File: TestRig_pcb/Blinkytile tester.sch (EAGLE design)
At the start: 142 parts, among them IC1 LM317BD2T, IC10 LM317BD2T, IC11 LM317BD2T, IC12 LM317BD2T, IC13 LM317BD2T, IC14 LM317BD2T, IC15 LM317BD2T, IC16 LM317BD2T, IC2 LM317BD2T, IC3 LM317BD2T, IC4 LM317BD2T, IC5 LM317BD2T, IC6 LM317BD2T, IC7 LM317BD2T, IC8 LM317BD2T, IC9 LM317BD2T, X1 MINI-USB_4P-85-32004-10X

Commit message: RevB of tester board: add 5v buffers
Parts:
- removed C1, C10, C11, C12, C13, C14, C15, C16, C17, C18, C19, C2, C20, C21, C22, C23, C24, C25, C26, C27, C28, C29, C3, C30, C31, C32, C4, C5, C6, C7, C8, C9: 0.1uF, rcl:C-EUC0805
- removed IC1, IC10, IC11, IC12, IC13, IC14, IC15, IC16, IC2, IC3, IC4, IC5, IC6, IC7, IC8, IC9: LM317BD2T, v-reg:LM317BD2T
- removed LED1, LED10, LED11, LED12, LED13, LED14, LED15, LED16, LED2, LED3, LED4, LED5, LED6, LED7, LED8, LED9: RED, adafruit:LED5MM
- removed R15, R16, R17, R18, R19, R20, R21, R22, R23, R24, R25, R26, R27, R28, R29, R30, R31, R32: (no value), rcl:R-EU_M0805
- removed SL16, SL17: (no value), con-amp-quick:M04
- removed TP1, TP10, TP11, TP12, TP13, TP14, TP15, TP16, TP2, TP3, TP4, TP5, TP6, TP7, TP8, TP9: TPPAD1-13Y, testpad:TPPAD1-13Y
- added SW1: SPST_TACT-EVQQ2, adafruit:SPST_TACT-EVQQ2
- added T1: (no value), zetex:PMOSSOT223
- added U1, U3: SN74HCT245PWR, scanlime:74245PW
- R1, R10, R11, R12, R13, R14, R2, R3, R4, R5, R6, R7, R8, R9: value (none) -> 50; device rcl:R-EU_M0805 -> adafruit:R-US_R0603
- renumbered LED17 to PASS, LED18 to FAIL, SL10 to OUT_9, SL11 to OUT_10, SL12 to OUT_11, SL13 to OUT_12, SL14 to OUT_13, SL15 to OUT_14, SL18 to SWITCH, SL2 to OUT_1, SL3 to OUT_2, SL4 to OUT_3, SL5 to OUT_4, SL6 to OUT_5, SL7 to OUT_6, SL8 to OUT_7, SL9 to OUT_8
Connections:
- net N$51 renamed GOOD
- removed net ADDR15: SL16.2, U$1.2
- removed net ADDR16: SL17.2, U$1.1
- removed net N$10: IC4.OUT, R7.1
- removed net N$12: LED4.C, R8.2
- removed net N$13: IC5.OUT, R9.1
- removed net N$14: C9.1, IC5.ADJ, LED5.A, OUT_5.1, R9.2, TP5.TP
- removed net N$15: LED5.C, R10.2
- removed net N$16: IC6.OUT, R11.1
- removed net N$18: LED6.C, R12.2
- removed net N$19: IC7.OUT, R13.1
- removed net N$21: LED7.C, R14.2
- removed net N$22: IC8.OUT, R15.1
- removed net N$24: LED8.C, R16.2
- removed net N$25: IC9.OUT, R17.1
- removed net N$27: LED9.C, R18.2
- removed net N$28: IC10.OUT, R19.1
- removed net N$30: LED10.C, R20.2
- removed net N$31: IC11.OUT, R21.1
- removed net N$33: LED11.C, R22.2
- removed net N$34: IC12.OUT, R23.1
- removed net N$35: C23.1, IC12.ADJ, LED12.A, OUT_12.1, R23.2, TP12.TP
- removed net N$36: LED12.C, R24.2
- removed net N$37: IC13.OUT, R25.1
- removed net N$39: LED13.C, R26.2
- removed net N$40: IC14.OUT, R27.1
- removed net N$42: LED14.C, R28.2
- removed net N$43: IC15.OUT, R29.1
- removed net N$45: LED15.C, R30.2
- removed net N$46: IC16.OUT, R31.1
- removed net N$47: C31.1, IC16.ADJ, LED16.A, R31.2, SL17.1, TP16.TP
- removed net N$48: LED16.C, R32.2
- removed net N$5: LED1.C, R2.2
- removed net N$54: SWITCH.2, U$1.9
- removed net N$6: LED2.C, R4.2
- removed net N$7: IC3.OUT, R5.1
- removed net N$9: LED3.C, R6.2
- new net 5V_B: R1.1, R10.1, R11.1, R12.1, R13.1, R14.1, R2.1, R3.1, R4.1, R5.1, R6.1, R7.1, R8.1, R9.1, T1.D
- new net ADDR10_B: OUT_10.2, U1.B2
- new net ADDR11_B: OUT_11.2, U1.B3
- new net ADDR12_B: OUT_12.2, U1.B4
- new net ADDR13_B: OUT_13.2, U1.B5
- new net ADDR14_B: OUT_14.2, U1.B6
- new net ADDR1_B: OUT_1.2, U3.B1
- new net ADDR2_B: OUT_2.2, U3.B2
- new net ADDR3_B: OUT_3.2, U3.B3
- new net ADDR4_B: OUT_4.2, U3.B4
- new net ADDR5_B: OUT_5.2, U3.B5
- new net ADDR6_B: OUT_6.2, U3.B6
- new net ADDR7_B: OUT_7.2, U3.B7
- new net ADDR8_B: OUT_8.2, U3.B8
- new net ADDR9_B: OUT_9.2, U1.B1
- new net DATA_B: OUT_1.3, OUT_10.3, OUT_11.3, OUT_12.3, OUT_13.3, OUT_14.3, OUT_2.3, OUT_3.3, OUT_4.3, OUT_5.3, OUT_6.3, OUT_7.3, OUT_8.3, OUT_9.3, U1.B8
- new net PWR_EN: U$1.2, U1.A7
- new net PWR_EN_B: T1.G, U1.B7
- net +5V: now also T1.S, U1.DIR, U1.OE, U1.VCC, U3.DIR, U3.OE, U3.VCC; no longer C1.1, C10.1, C12.1, C14.1, C16.1, C18.1, C20.1, C22.1, C24.1, C26.1, C28.1, C30.1, C32.1, C4.1, C6.1, C8.1, IC1.IN, IC10.IN, IC11.IN, IC12.IN, IC13.IN, IC14.IN, IC15.IN, IC16.IN, IC2.IN, IC3.IN, IC4.IN, IC5.IN, IC6.IN, IC7.IN, IC8.IN, IC9.IN
- net ADDR1: now also U3.A1; no longer OUT_1.2
- net ADDR10: now also U1.A2; no longer OUT_10.2
- net ADDR11: now also U1.A3; no longer OUT_11.2
- net ADDR12: now also U1.A4; no longer OUT_12.2
- net ADDR13: now also U1.A5; no longer OUT_13.2
- net ADDR14: now also U1.A6; no longer OUT_14.2
- net ADDR2: now also U3.A2; no longer OUT_2.2
- net ADDR3: now also U3.A3; no longer OUT_3.2
- net ADDR4: now also U3.A4; no longer OUT_4.2
- net ADDR5: now also U3.A5; no longer OUT_5.2
- net ADDR6: now also U3.A6; no longer OUT_6.2
- net ADDR7: now also U3.A7; no longer OUT_7.2
- net ADDR8: now also U3.A8; no longer OUT_8.2
- net ADDR9: now also U1.A1; no longer OUT_9.2
- net DATA: now also U1.A8; no longer OUT_1.3, OUT_10.3, OUT_11.3, OUT_12.3, OUT_13.3, OUT_14.3, OUT_2.3, OUT_3.3, OUT_4.3, OUT_5.3, OUT_6.3, OUT_7.3, OUT_8.3, OUT_9.3, SL16.3, SL17.3
- net GND: now also SW1.P, SW1.P1, U1.GND, U3.GND; no longer C1.2, C10.2, C11.2, C12.2, C13.2, C14.2, C15.2, C16.2, C17.2, C18.2, C19.2, C2.2, C20.2, C21.2, C22.2, C23.2, C24.2, C25.2, C26.2, C27.2, C28.2, C29.2, C3.2, C30.2, C31.2, C32.2, C4.2, C5.2, C6.2, C7.2, C8.2, C9.2, R10.1, R12.1, R14.1, R16.1, R18.1, R2.1, R20.1, R22.1, R24.1, R26.1, R28.1, R30.1, R32.1, R4.1, R6.1, R8.1, SL16.4, SL17.4
- net N$1: now also OUT_5.1, R5.2; no longer IC1.OUT, R1.1
- net N$11: now also R4.2; no longer C7.1, IC4.ADJ, LED4.A, R7.2, TP4.TP
- net N$17: now also R6.2; no longer C11.1, IC6.ADJ, LED6.A, R11.2, TP6.TP
- net N$2: no longer C2.1, IC1.ADJ, LED1.A, TP1.TP
- net N$20: now also R7.2; no longer C13.1, IC7.ADJ, LED7.A, R13.2, TP7.TP
- net N$23: now also R8.2; no longer C15.1, IC8.ADJ, LED8.A, R15.2, TP8.TP
- net N$26: now also R9.2; no longer C17.1, IC9.ADJ, LED9.A, R17.2, TP9.TP
- net N$29: now also R10.2; no longer C19.1, IC10.ADJ, LED10.A, R19.2, TP10.TP
- net N$3: now also SW1.S, SW1.S1, SWITCH.2, U$1.9; no longer IC2.OUT, R3.1
- net N$32: now also R11.2; no longer C21.1, IC11.ADJ, LED11.A, R21.2, TP11.TP
- net N$38: now also R13.2; no longer C25.1, IC13.ADJ, LED13.A, R25.2, TP13.TP
- net N$4: now also R2.2; no longer C3.1, IC2.ADJ, LED2.A, R3.2, TP2.TP
- net N$41: now also R14.2; no longer C27.1, IC14.ADJ, LED14.A, R27.2, TP14.TP
- net N$44: now also OUT_12.1, R12.2; no longer C29.1, IC15.ADJ, LED15.A, R29.2, SL16.1, TP15.TP
- net N$8: now also R3.2; no longer C5.1, IC3.ADJ, LED3.A, R5.2, TP3.TP

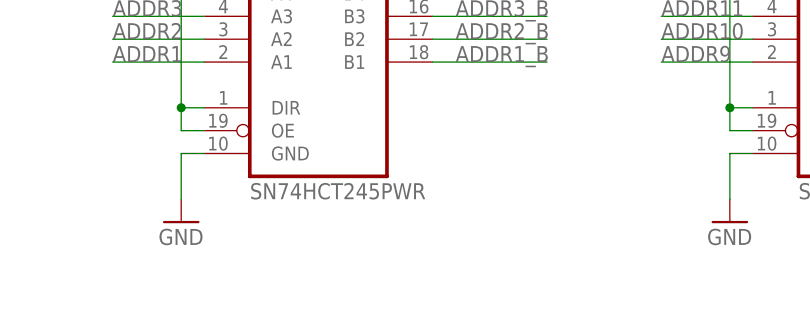
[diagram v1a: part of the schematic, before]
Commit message: Getting the tile test rig working: small circuit design issues.
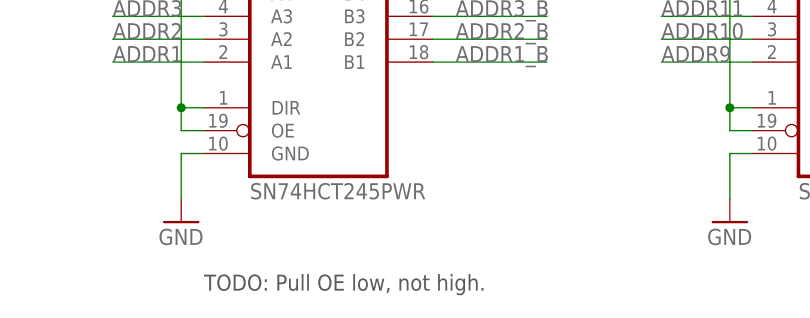
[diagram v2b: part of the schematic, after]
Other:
- note added: "TODO: Pull OE low, not high."
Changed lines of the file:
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@@
 <sheet>
 <plain>
+<text x="-20.32" y="-101.6" size="1.778" layer="97">TODO: Pull OE low, not high.</text>
 </plain>
 <instances>
